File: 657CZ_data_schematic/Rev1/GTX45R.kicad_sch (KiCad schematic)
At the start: 2 parts

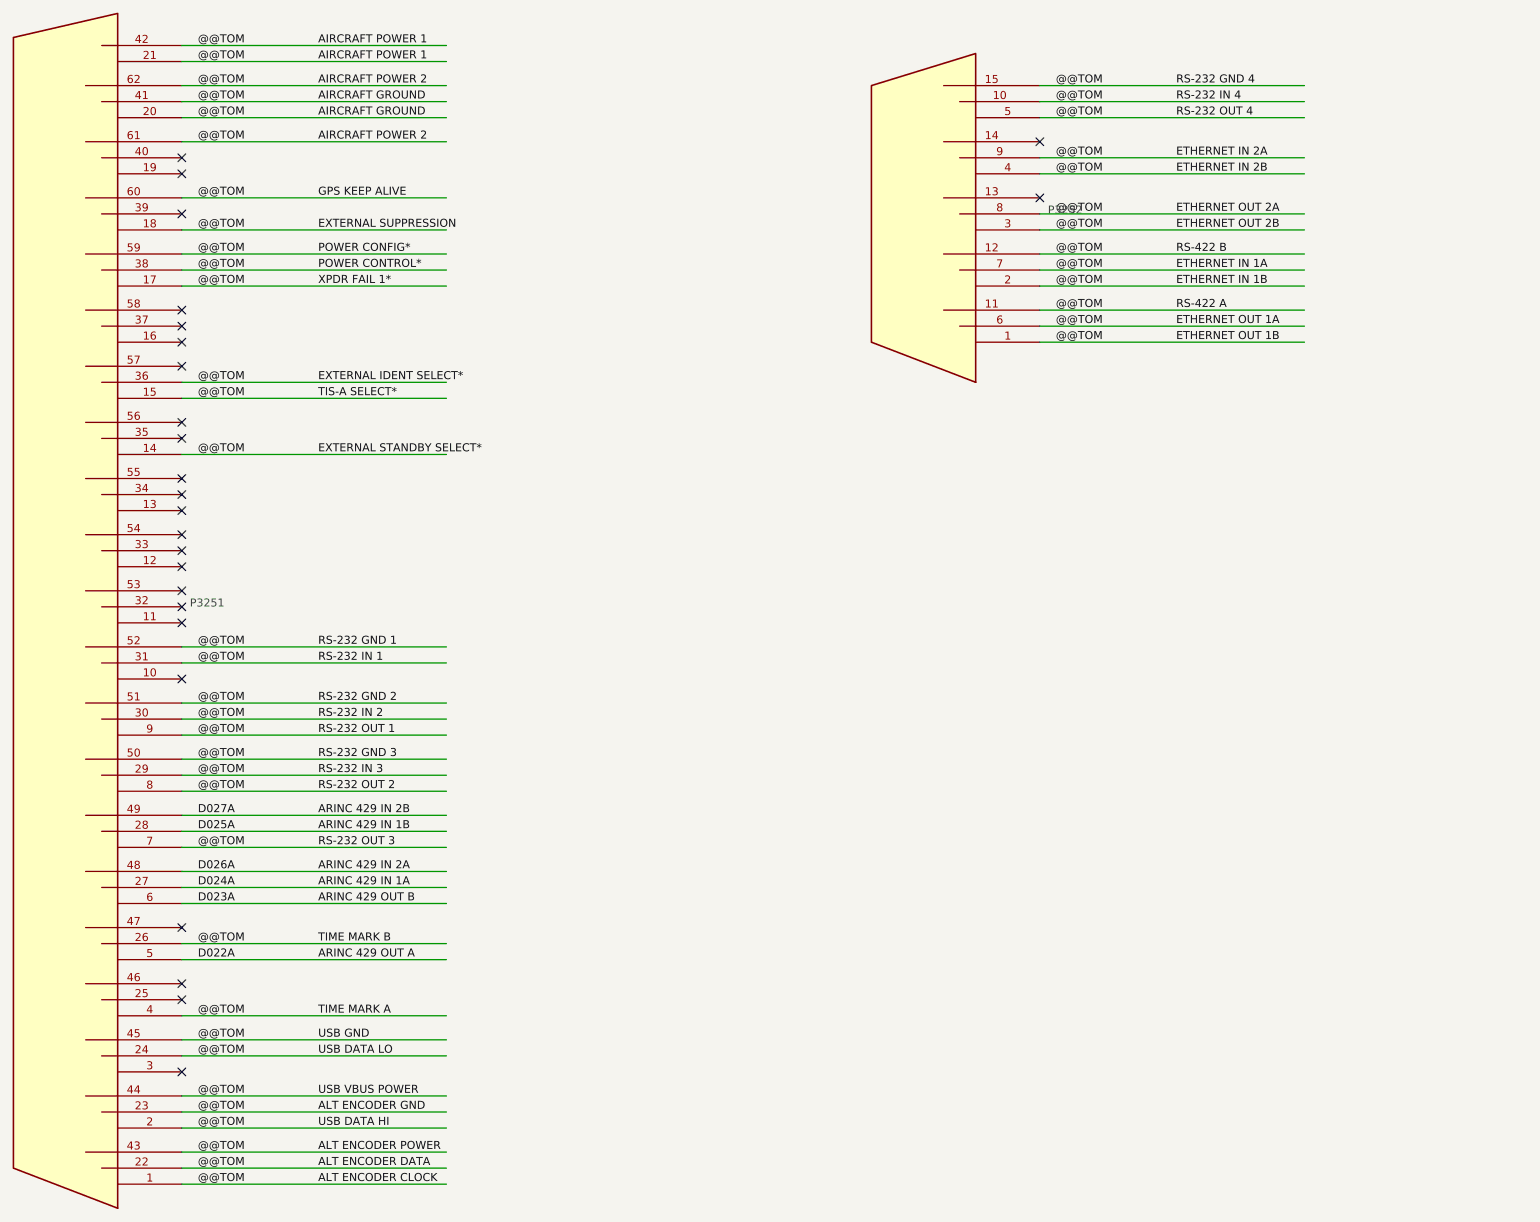
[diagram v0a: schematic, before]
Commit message: added data connections after AvClassics wiring. completed LRUs GMU, GDU, GSU, GAD, GNC, GTX, GTR  Not completed GMA, GEA and autopilot LRUs
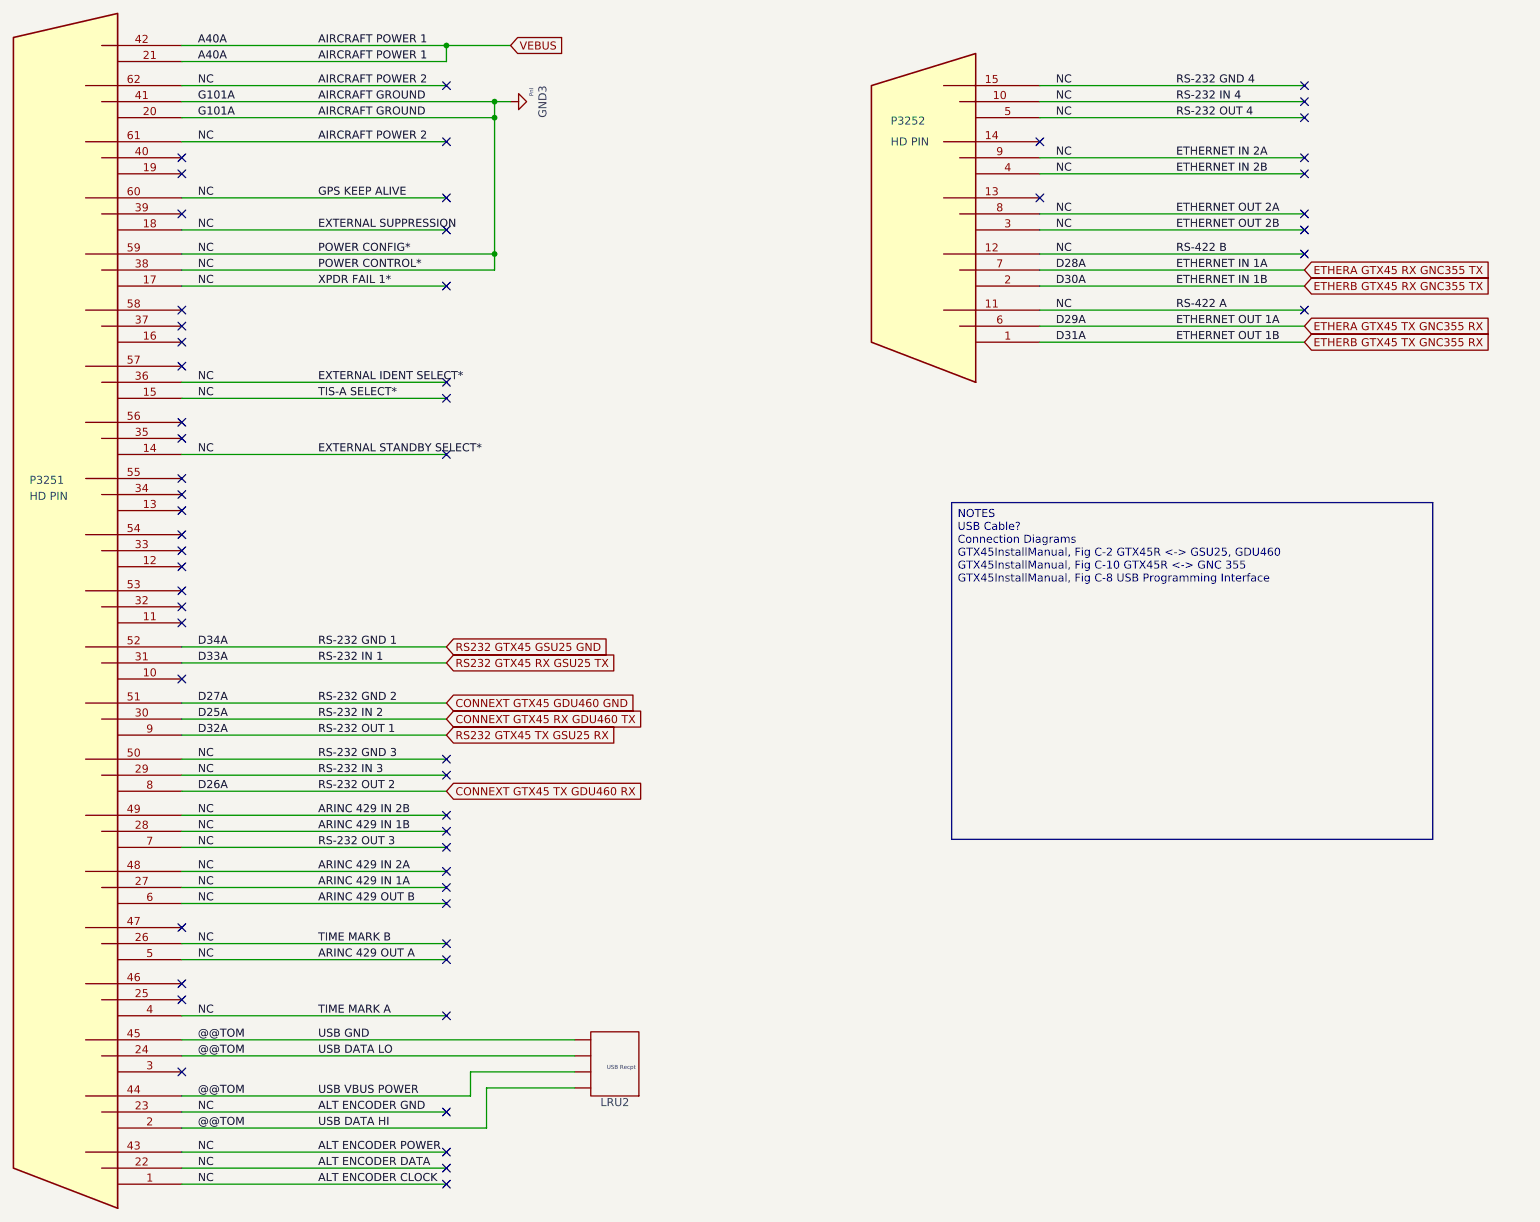
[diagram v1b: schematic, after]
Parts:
- added LRU2: USB Recpt, symbol AeroElectricConnectionSymbols:LRU_4x
- P3251, P3252: value ~ -> HD PIN
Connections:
- net @@TOM: now also LRU2.1 (Red), LRU2.2 (Blk), LRU2.3 (Ylw), LRU2.4 (Blu)
- no-connect marks 25 -> 57
